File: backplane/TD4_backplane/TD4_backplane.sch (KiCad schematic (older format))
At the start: 20 parts, among them J1 Conn_02x32_Row_Letter_First, J10 Conn_02x32_Row_Letter_First, J11 Conn_02x32_Row_Letter_First, J12 Conn_02x32_Row_Letter_First, J13 Conn_02x32_Row_Letter_First, J14 Conn_02x32_Row_Letter_First, J15 Conn_02x32_Row_Letter_First, J16 Conn_02x32_Row_Letter_First, J17 Conn_02x32_Row_Letter_First, J18 Conn_02x32_Row_Letter_First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

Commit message: Backplane routed
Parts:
- removed J10, J11, J12, J13, J14, J15, J16, J17, J18, J19, J20, J6, J7, J8, J9: Conn_02x32_Row_Letter_First, symbol Connector_Generic:Conn_02x32_Row_Letter_First
- added J6: Barrel_Jack_Switch, Connector_BarrelJack:BarrelJack_Horizontal, symbol Connector:Barrel_Jack_Switch
- J1, J2, J3, J4, J5: footprint (none) -> Connector_DIN:DIN41612_B_2x32_Vertical
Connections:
- net GND: now also J6.2
- net VCC: now also J6.1
- no-connect marks 0 -> 1

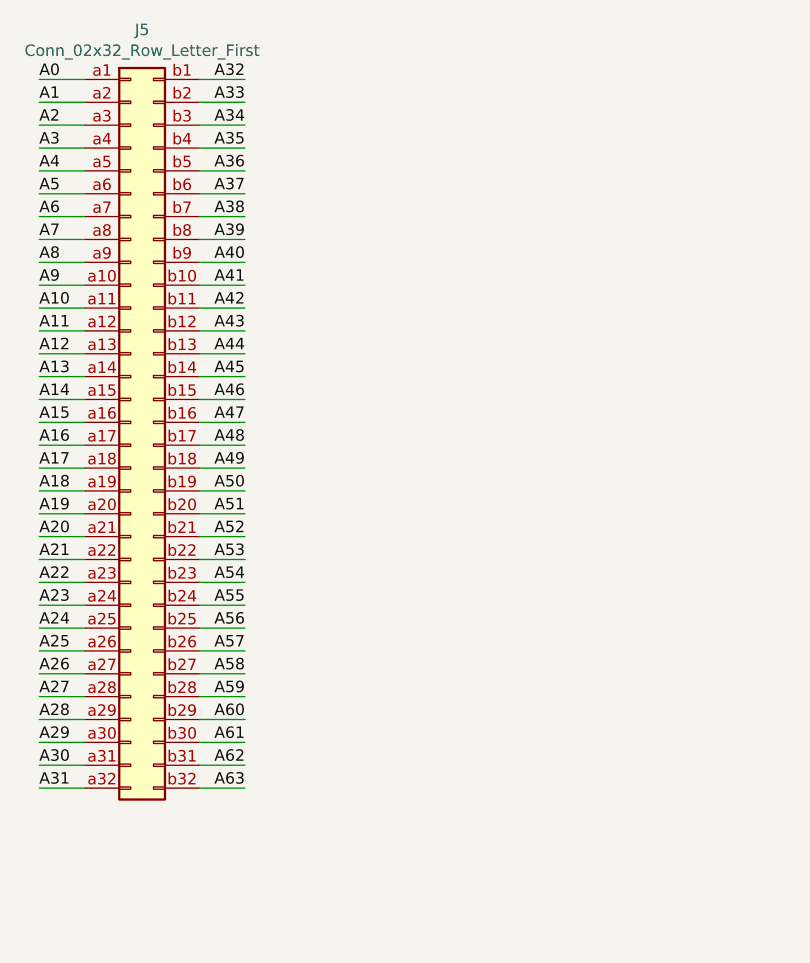
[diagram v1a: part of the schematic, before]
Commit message: Added 6th slot to the backplane
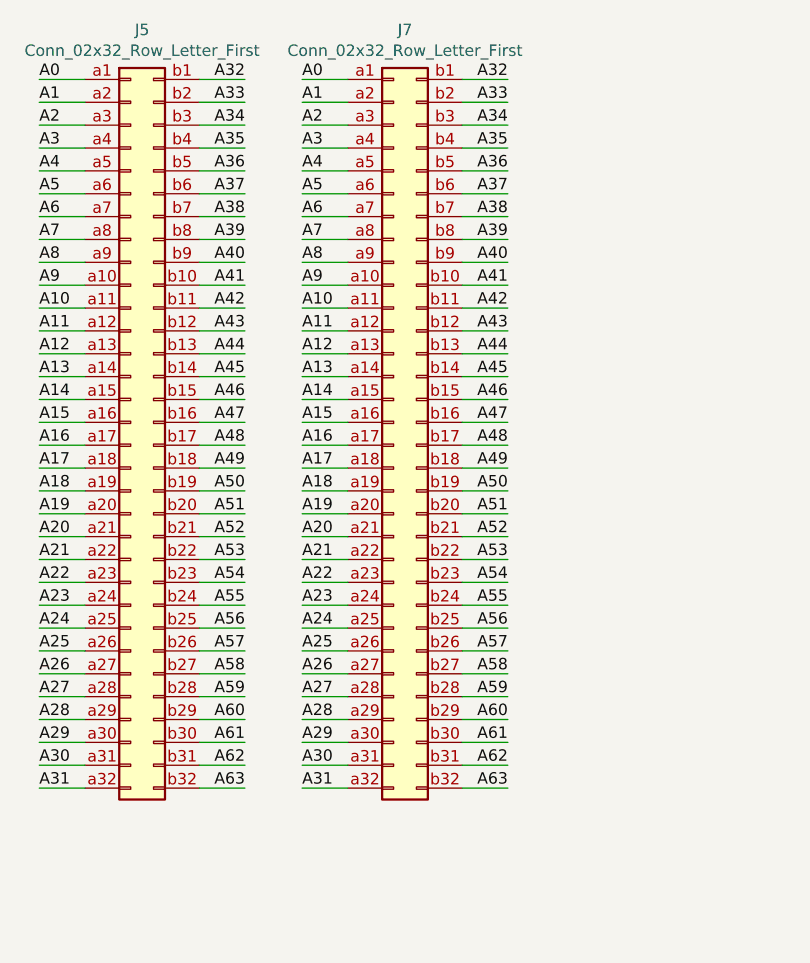
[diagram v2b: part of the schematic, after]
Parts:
- added J7: Conn_02x32_Row_Letter_First, Connector_DIN:DIN41612_B_2x32_Vertical, symbol Connector_Generic:Conn_02x32_Row_Letter_First
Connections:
- net A10: now also J7.a11 (Pin_a11)
- net A11: now also J7.a12 (Pin_a12)
- net A12: now also J7.a13 (Pin_a13)
- net A13: now also J7.a14 (Pin_a14)
- net A14: now also J7.a15 (Pin_a15)
- net A15: now also J7.a16 (Pin_a16)
- net A16: now also J7.a17 (Pin_a17)
- net A17: now also J7.a18 (Pin_a18)
- net A2: now also J7.a3 (Pin_a3)
- net A20: now also J7.a21 (Pin_a21)
- net A21: now also J7.a22 (Pin_a22)
- net A22: now also J7.a23 (Pin_a23)
- net A23: now also J7.a24 (Pin_a24)
- net A24: now also J7.a25 (Pin_a25)
- net A25: now also J7.a26 (Pin_a26)
- net A26: now also J7.a27 (Pin_a27)
- net A27: now also J7.a28 (Pin_a28)
- net A28: now also J7.a29 (Pin_a29)
- net A29: now also J7.a30 (Pin_a30)
- net A3: now also J7.a4 (Pin_a4)
- net A34: now also J7.b3 (Pin_b3)
- net A35: now also J7.b4 (Pin_b4)
- net A36: now also J7.b5 (Pin_b5)
- net A37: now also J7.b6 (Pin_b6)
- net A38: now also J7.b7 (Pin_b7)
- net A39: now also J7.b8 (Pin_b8)
- net A4: now also J7.a5 (Pin_a5)
- net A40: now also J7.b9 (Pin_b9)
- net A41: now also J7.b10 (Pin_b10)
- net A42: now also J7.b11 (Pin_b11)
- net A43: now also J7.b12 (Pin_b12)
- net A44: now also J7.b13 (Pin_b13)
- net A45: now also J7.b14 (Pin_b14)
- net A46: now also J7.b15 (Pin_b15)
- net A47: now also J7.b16 (Pin_b16)
- net A48: now also J7.b17 (Pin_b17)
- net A49: now also J7.b18 (Pin_b18)
- net A5: now also J7.a6 (Pin_a6)
- net A52: now also J7.b21 (Pin_b21)
- net A53: now also J7.b22 (Pin_b22)
- net A54: now also J7.b23 (Pin_b23)
- net A55: now also J7.b24 (Pin_b24)
- net A56: now also J7.b25 (Pin_b25)
- net A57: now also J7.b26 (Pin_b26)
- net A58: now also J7.b27 (Pin_b27)
- net A59: now also J7.b28 (Pin_b28)
- net A6: now also J7.a7 (Pin_a7)
- net A60: now also J7.b29 (Pin_b29)
- net A61: now also J7.b30 (Pin_b30)
- net A7: now also J7.a8 (Pin_a8)
- net A8: now also J7.a9 (Pin_a9)
- net A9: now also J7.a10 (Pin_a10)
- net GND: now also J7.a1 (Pin_a1), J7.a19 (Pin_a19), J7.a32 (Pin_a32), J7.b1 (Pin_b1), J7.b19 (Pin_b19), J7.b32 (Pin_b32)
- net VCC: now also J7.a2 (Pin_a2), J7.a20 (Pin_a20), J7.a31 (Pin_a31), J7.b2 (Pin_b2), J7.b20 (Pin_b20), J7.b31 (Pin_b31)
